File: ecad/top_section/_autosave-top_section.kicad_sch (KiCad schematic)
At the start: 11 parts, among them J1 JST PH, J2 JST PH, J3 JST SH, U11 MCP23017_ML

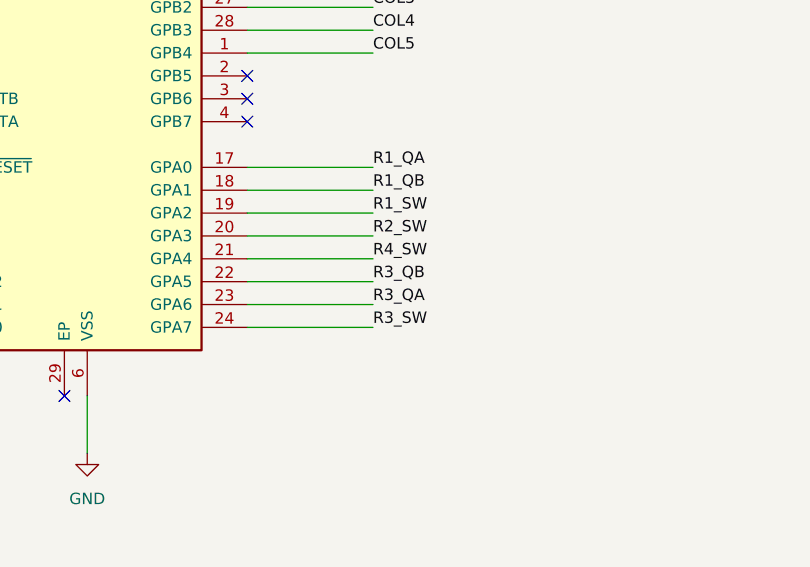
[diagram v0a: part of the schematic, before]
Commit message: Uses WS2811 led communication everywhere
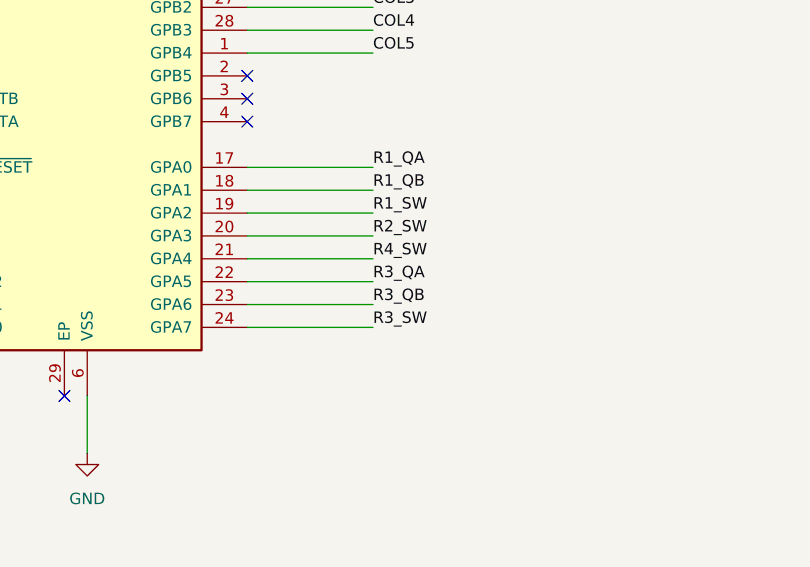
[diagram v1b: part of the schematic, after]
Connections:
- net R3_QA: now also U11.22 (GPA5); no longer U11.23 (GPA6)
- net R3_QB: now also U11.23 (GPA6); no longer U11.22 (GPA5)
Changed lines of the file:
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@@
 	)
 	(label "R3_QA"
-		(at 125.73 224.79 0)
+		(at 125.73 222.25 0)
 		(effects
 			(font
@@
 	)
 	(label "R3_QB"
-		(at 125.73 222.25 0)
-		(effects
-			(font
+		(at 125.73 224.79 0)
+		(effects
+			(font
